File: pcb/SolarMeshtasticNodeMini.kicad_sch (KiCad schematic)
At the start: 32 parts, among them J1 Conn_01x02_Socket, J2 Conn_01x02_Socket, J3 Conn_01x04_Socket, J4 Conn_01x02_Pin, J5 Conn_01x04_Socket, SW1 SSSS811101, SW2 SW_Push, U1 BQ25185, U2 HT-CT62, U3 HE9073A30MR, U4 APX803L05-32SA-7, U9 SS26_C5350986

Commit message: pcb, sch: first layout done
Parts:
- removed J1: Conn_01x02_Socket, Connector_JST:JST_PH_B2B-PH-K_1x02_P2.00mm_Vertical, symbol Connector:Conn_01x02_Pin
- C7: value C -> 1uF
- R1: footprint (none) -> Resistor_SMD:R_0805_2012Metric_Pad1.20x1.40mm_HandSolder
- R6: footprint footprints:RES-TH_L6.5-W4.0-P2.50-D0.5 -> Resistor_SMD:R_0805_2012Metric_Pad1.20x1.40mm_HandSolder
- SW2: footprint (none) -> footprints:SMA_L4.3-W2.6-LS5.1-RD
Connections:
- net GND: now also J2.2 (Pin_2), J4.2 (Pin_2); no longer J2.1 (Pin_1), J4.1 (Pin_1)
- net VBUS: now also J2.1 (Pin_1); no longer J2.2 (Pin_2)
- net VLIPO: now also J4.1 (Pin_1); no longer J4.2 (Pin_2)
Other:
- note removed: "LiPo Panel Connection"
- note removed: "Microcontroller"
- moved on the sheet: C15, J2, R1, R13, R14, SW1

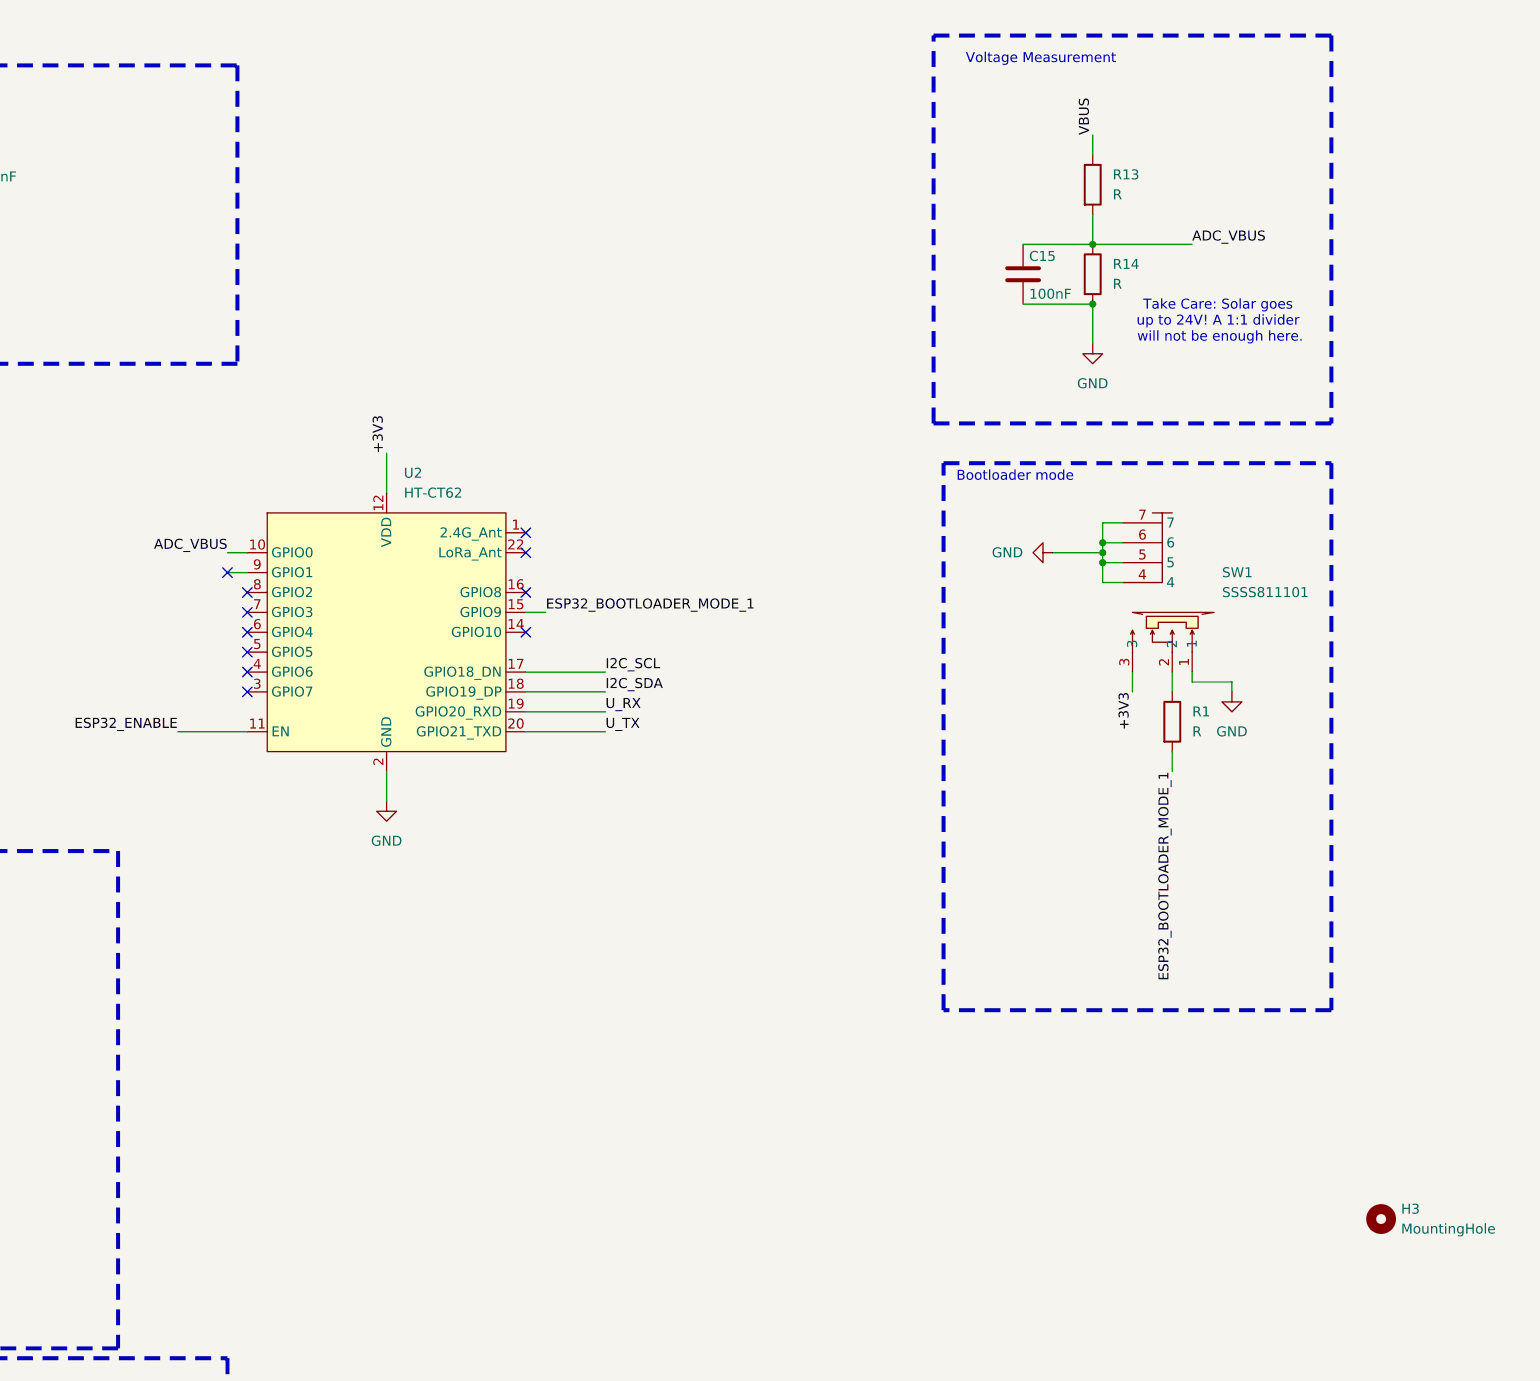
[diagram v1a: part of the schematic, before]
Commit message: pcb, sch: use VLOAD and not VBUS for ADC
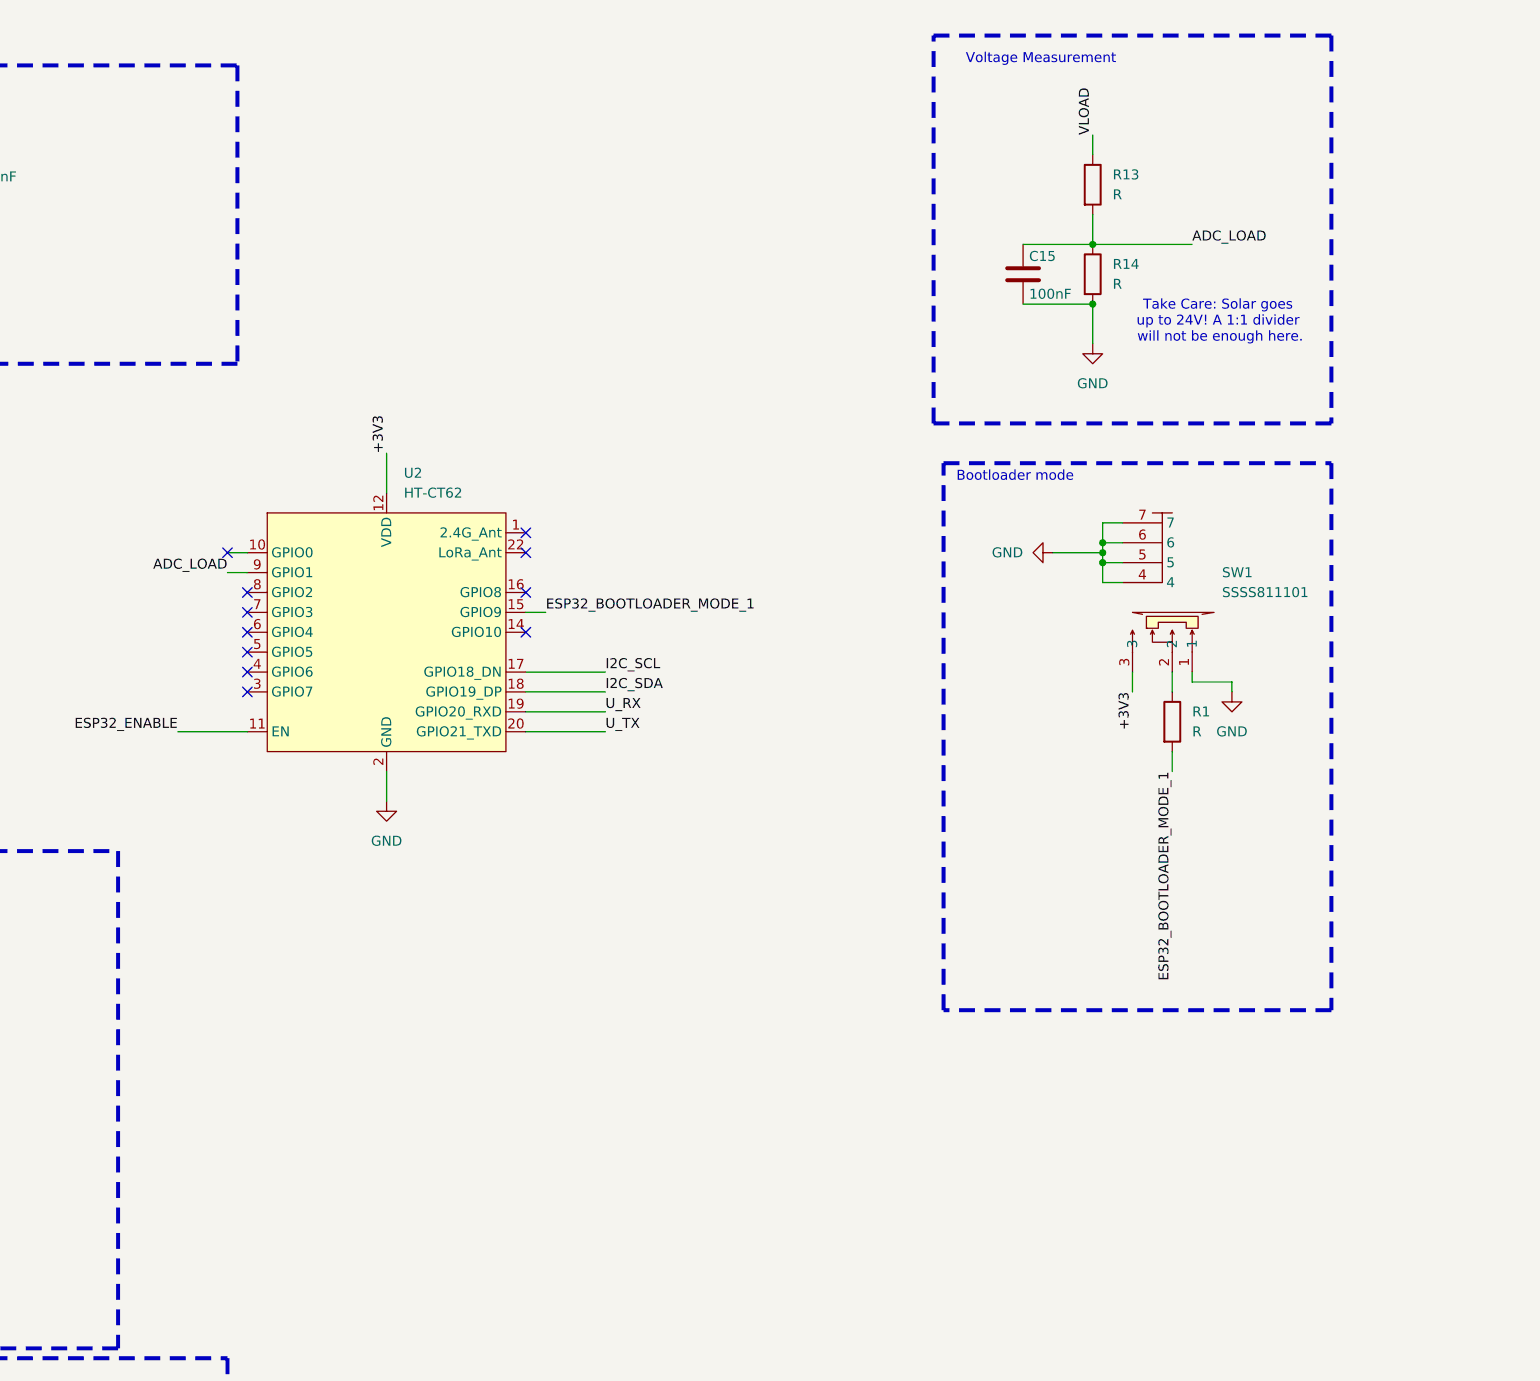
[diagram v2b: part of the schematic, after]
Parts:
- removed H3: MountingHole, MountingHole:MountingHole_4.3mm_M4_DIN965, symbol Mechanical:MountingHole
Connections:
- net VBUS: no longer R13.1
- net VLOAD: now also R13.1
- net ADC_LOAD: now reaches U2.9 (GPIO1)
- net ADC_LOAD: now also C15.1, R13.2, R14.1
- removed net ADC_VBUS: C15.1, R13.2, R14.1, U2.10 (GPIO0)
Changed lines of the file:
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@@
 	)
 	(no_connect
-		(at 180.34 83.82)
+		(at 180.34 81.28)
 	)
 	(no_connect
@@
 		)
 	)
-	(label "ADC_VBUS"
-		(at 180.34 81.28 180)
-		(effects
-			(font
-				(size 1.27 1.27)
-			)
-			(justify right bottom)
-		)
-	)
 	(label "GND"
 		(at 69.85 170.18 90)
@@
 		)
 	)
-	(label "ADC_VBUS"
+	(label "ADC_LOAD"
 		(at 303.53 41.91 0)
 		(effects
@@
 		)
 	)
-	(label "VBUS"
+	(label "VLOAD"
 		(at 290.83 27.94 90)
 		(effects
@@
 		)
 	)
+	(label "ADC_LOAD"
+		(at 180.34 83.82 180)
+		(effects
+			(font
+				(size 1.27 1.27)
+			)
+			(justify right bottom)
+		)
+	)
 	(symbol
 		(lib_id "power:GND")
@@
 					(unit 1)
 				)
-			)
-		)
-	)
-	(symbol
-		(lib_id "Mechanical:MountingHole")
-		(at 327.66 166.37 0)
-		(unit 1)
-		(exclude_from_sim yes)
-		(in_bom no)
-		(on_board yes)
-		(dnp no)
-		(property "Reference" "H3"
-			(at 330.2 165.0999 0)
-			(effects
-				(font
-					(size 1.27 1.27)
-				)
-				(justify left)
-			)
-		)
-		(property "Value" "MountingHole"
-			(at 330.2 167.6399 0)
-			(effects
-				(font
-					(size 1.27 1.27)
-				)
-				(justify left)
-			)
-		)
-		(property "Footprint" "MountingHole:MountingHole_4.3mm_M4_DIN965"
-			(at 327.66 166.37 0)
-			(effects
-				(font
-					(size 1.27 1.27)
-				)
-				(hide yes)
-			)
-		)
-		(property "Datasheet" "~"
-			(at 327.66 166.37 0)
-			(effects
-				(font
-					(size 1.27 1.27)
-				)
-				(hide yes)
-			)
-		)
-		(property "Description" "Mounting Hole without connection"
-			(at 327.66 166.37 0)
-			(effects
-				(font
-					(size 1.27 1.27)
-				)
-				(hide yes)
-			)
-		)
-		(property "Sim.Device" ""
-			(at 327.66 166.37 0)
-			(effects
-				(font
-					(size 1.27 1.27)
-				)
-				(hide yes)
-			)
-		)
-		(property "Sim.Pins" ""
-			(at 327.66 166.37 0)
-			(effects
-				(font
-					(size 1.27 1.27)
-				)
-				(hide yes)
-			)
-		)
-		(property "Sim.Type" ""
-			(at 327.66 166.37 0)
-			(effects
-				(font
-					(size 1.27 1.27)
-				)
-				(hide yes)
-			)
-		)
-		(instances
-			(project "MeshtasticNode"
-				(path "/256f162e-4f54-42b3-a315-b65231ce36a5"
-					(reference "H3")
-					(unit 1)
-				)

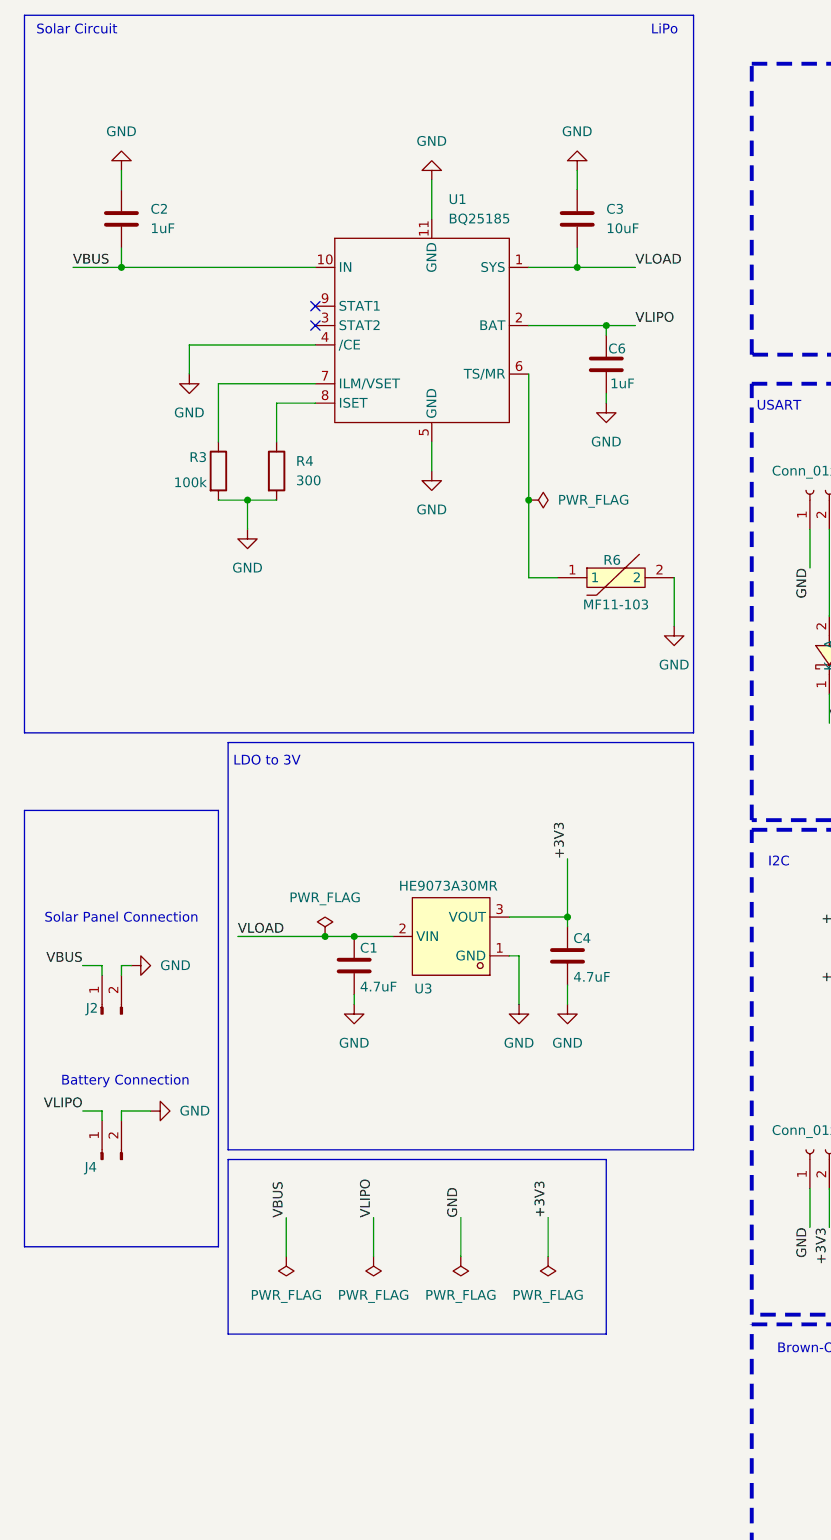
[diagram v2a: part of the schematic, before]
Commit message: pcb, sch: add mounting hole (M2.5)
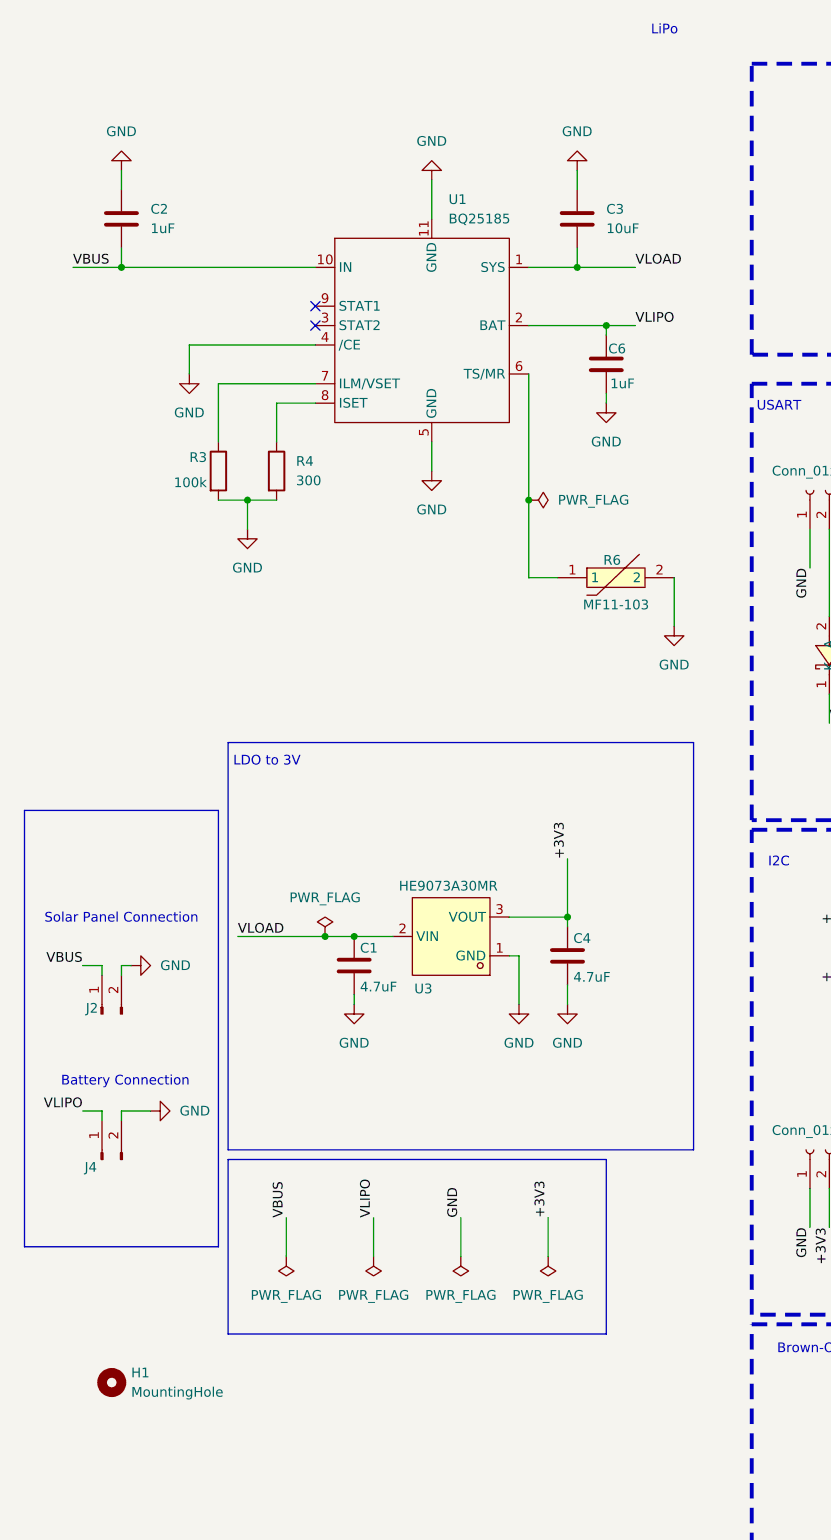
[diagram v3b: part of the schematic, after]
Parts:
- added H1: MountingHole, MountingHole:MountingHole_2.7mm_M2.5_ISO14580_Pad_TopBottom, symbol Mechanical:MountingHole
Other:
- note removed: "Solar Circuit"
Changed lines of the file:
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@@
 	)
 	(rectangle
-		(start 12.7 12.7)
-		(end 100.33 106.68)
-		(stroke
-			(width 0)
-			(type default)
-		)
-		(fill
-			(type none)
-		)
-	)
-	(rectangle
 		(start 39.37 107.95)
 		(end 100.33 161.29)
@@
 		)
 	)
-	(text "Solar Circuit"
-		(exclude_from_sim no)
-		(at 19.558 14.732 0)
-		(effects
-			(font
-				(size 1.27 1.27)
-			)
-		)
-	)
 	(text "USART"
 		(exclude_from_sim no)
@@
 					(unit 1)
 				)
+			)
+		)
+	)
+	(symbol
+		(lib_id "Mechanical:MountingHole")
+		(at 24.13 191.77 0)
+		(unit 1)
+		(exclude_from_sim no)
+		(in_bom no)
+		(on_board yes)
+		(dnp no)
+		(fields_autoplaced yes)
+		(property "Reference" "H1"
+			(at 26.67 190.4999 0)
+			(effects
+				(font
+					(size 1.27 1.27)
+				)
+				(justify left)
+			)
+		)
+		(property "Value" "MountingHole"
+			(at 26.67 193.0399 0)
+			(effects
+				(font
+					(size 1.27 1.27)
+				)
+				(justify left)
+			)
+		)
+		(property "Footprint" "MountingHole:MountingHole_2.7mm_M2.5_ISO14580_Pad_TopBottom"
+			(at 24.13 191.77 0)
+			(effects
+				(font
+					(size 1.27 1.27)
+				)
+				(hide yes)
+			)
+		)
+		(property "Datasheet" "~"
+			(at 24.13 191.77 0)
+			(effects
+				(font
+					(size 1.27 1.27)
+				)
+				(hide yes)
+			)
+		)
+		(property "Description" "Mounting Hole without connection"
+			(at 24.13 191.77 0)
+			(effects
+				(font
+					(size 1.27 1.27)
+				)
+				(hide yes)
+			)
+		)
+		(instances
+			(project ""
+				(path "/256f162e-4f54-42b3-a315-b65231ce36a5"
+					(reference "H1")
+					(unit 1)
+				)

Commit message: pcb, sch: other hole size and re-center
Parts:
- H1: footprint MountingHole:MountingHole_2.7mm_M2.5_ISO14580_Pad_TopBottom -> MountingHole:MountingHole_2.7mm_M2.5_ISO7380
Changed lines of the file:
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@@
 			)
 		)
-		(property "Footprint" "MountingHole:MountingHole_2.7mm_M2.5_ISO14580_Pad_TopBottom"
+		(property "Footprint" "MountingHole:MountingHole_2.7mm_M2.5_ISO7380"
 			(at 24.13 191.77 0)
 			(effects
